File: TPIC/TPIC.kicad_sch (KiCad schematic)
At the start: 1 part, among them U1 4001

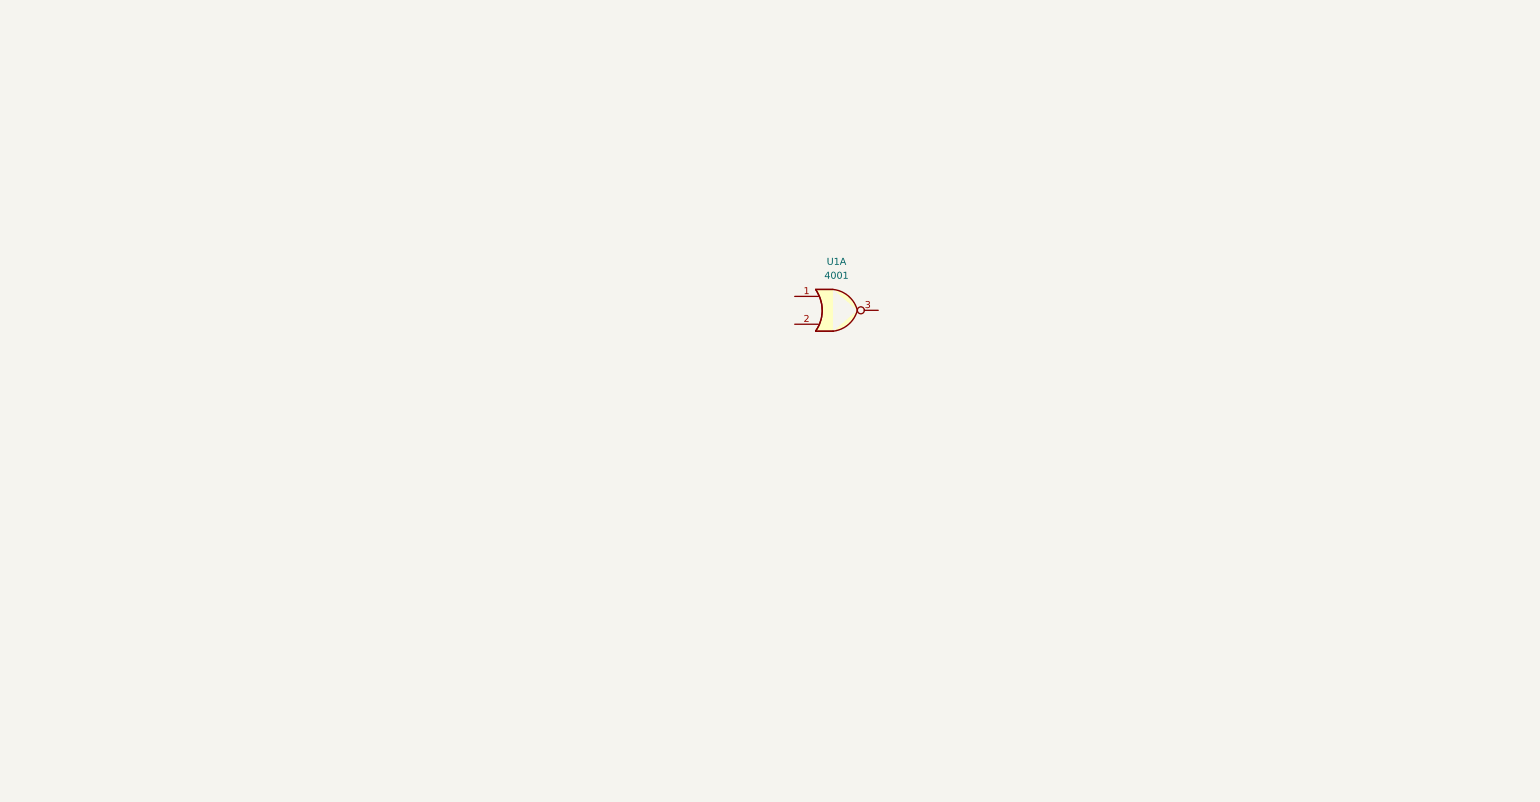
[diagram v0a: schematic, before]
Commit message: First schematic changes
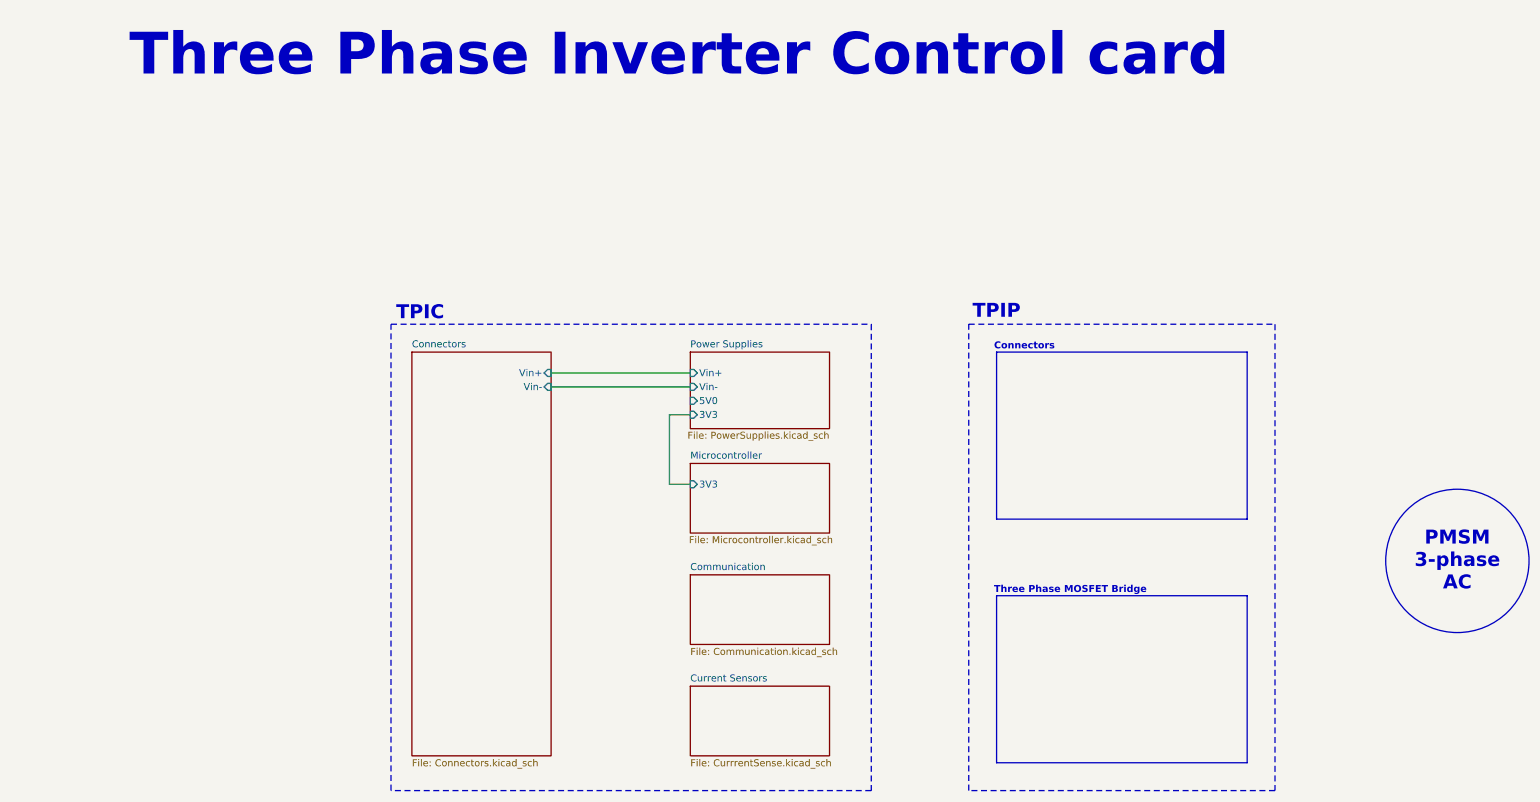
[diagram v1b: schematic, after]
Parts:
- removed U1: 4001, symbol 4xxx:4001
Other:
- added sheet Communication (Communication.kicad_sch)
- added sheet Connectors (Connectors.kicad_sch)
- added sheet Current Sensors (CurrrentSense.kicad_sch)
- added sheet Microcontroller (Microcontroller.kicad_sch)
- added sheet Power Supplies (PowerSupplies.kicad_sch)
- note added: "Connectors"
- note added: "PMSM 3-phase AC"
- note added: "TPIC"
- note added: "TPIP"
- note added: "Three Phase Inverter Control card"
- note added: "Three Phase MOSFET Bridge"
- company: (none) -> Ødegårdstuen Productions
- title: (none) -> Three Phase Inverter Control card
